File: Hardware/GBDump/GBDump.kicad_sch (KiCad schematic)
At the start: 19 parts, among them J1 Conn_01x06, J2 Micro_SD_Card_Det_Hirose_DM3AT, J3 Conn_01x06, U2 TXB0108PW, U3 TXB0108PW, U4 TXB0108PW, U5 Cartridge_Bus, U6 TXB0108PW

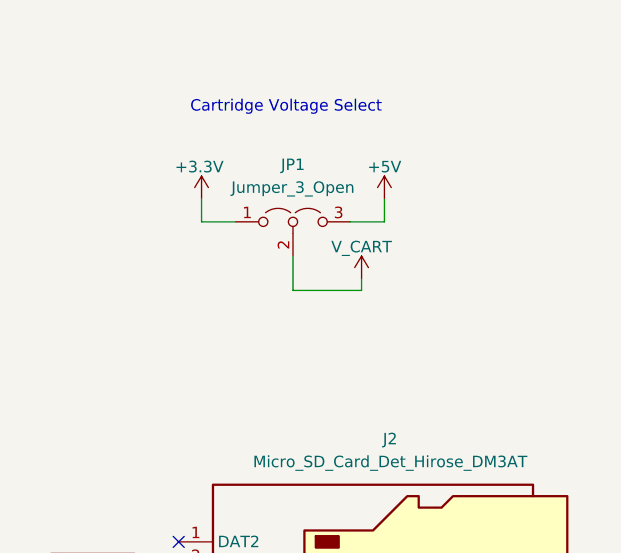
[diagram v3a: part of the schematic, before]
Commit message: Fixed CART_VCC label
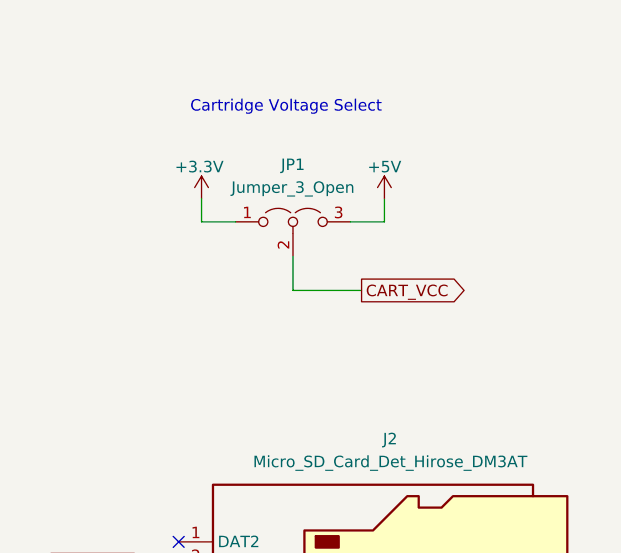
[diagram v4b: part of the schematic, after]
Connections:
- net CART_VCC: now also JP1.2 (C)
- net V_CART: no longer JP1.2 (C)
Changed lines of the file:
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@@
 	(wire
 		(pts
-			(xy 245.11 43.18) (xy 245.11 41.91)
-		)
-		(stroke
-			(width 0)
-			(type default)
-		)
-	)
-	(wire
-		(pts
 			(xy 130.81 78.74) (xy 175.26 78.74)
 		)
@@
 		)
 	)
+	(global_label "CART_VCC"
+		(shape output)
+		(at 245.11 43.18 0)
+		(fields_autoplaced yes)
+		(effects
+			(font
+				(size 1.27 1.27)
+			)
+			(justify left)
+		)
+		(property "Intersheetrefs" "${INTERSHEET_REFS}"
+			(at 257.2876 43.18 0)
+			(effects
+				(font
+					(size 1.27 1.27)
+				)
+				(justify left)
+				(hide yes)
+			)
+		)
+	)
 	(global_label "CART_WR"
 		(shape output)
@@
 					(unit 1)
 				)
-			)
-		)
-	)
-	(symbol
-		(lib_id "power:+3.3V")
-		(at 245.11 41.91 0)
-		(unit 1)
-		(exclude_from_sim no)
-		(in_bom yes)
-		(on_board yes)
-		(dnp no)
-		(property "Reference" "#PWR026"
-			(at 245.11 45.72 0)
-			(effects
-				(font
-					(size 1.27 1.27)
-				)
-				(hide yes)
-			)
-		)
-		(property "Value" "V_CART"
-			(at 245.11 38.354 0)
-			(effects
-				(font
-					(size 1.27 1.27)
-				)
-			)
-		)
-		(property "Footprint" ""
-			(at 245.11 41.91 0)
-			(effects
-				(font
-					(size 1.27 1.27)
-				)
-				(hide yes)
-			)
-		)
-		(property "Datasheet" ""
-			(at 245.11 41.91 0)
-			(effects
-				(font
-					(size 1.27 1.27)
-				)
-				(hide yes)
-			)
-		)
-		(property "Description" "Power symbol creates a global label with name \"+3.3V\""
-			(at 245.11 41.91 0)
-			(effects
-				(font
-					(size 1.27 1.27)
-				)
-				(hide yes)
-			)
-		)
-		(pin "1"
-		)
-		(instances
-			(project "GBDump"
-				(path "/97c582ec-aebc-49f1-a03f-b2d95e3214dc"
-					(reference "#PWR026")
-					(unit 1)
-				)

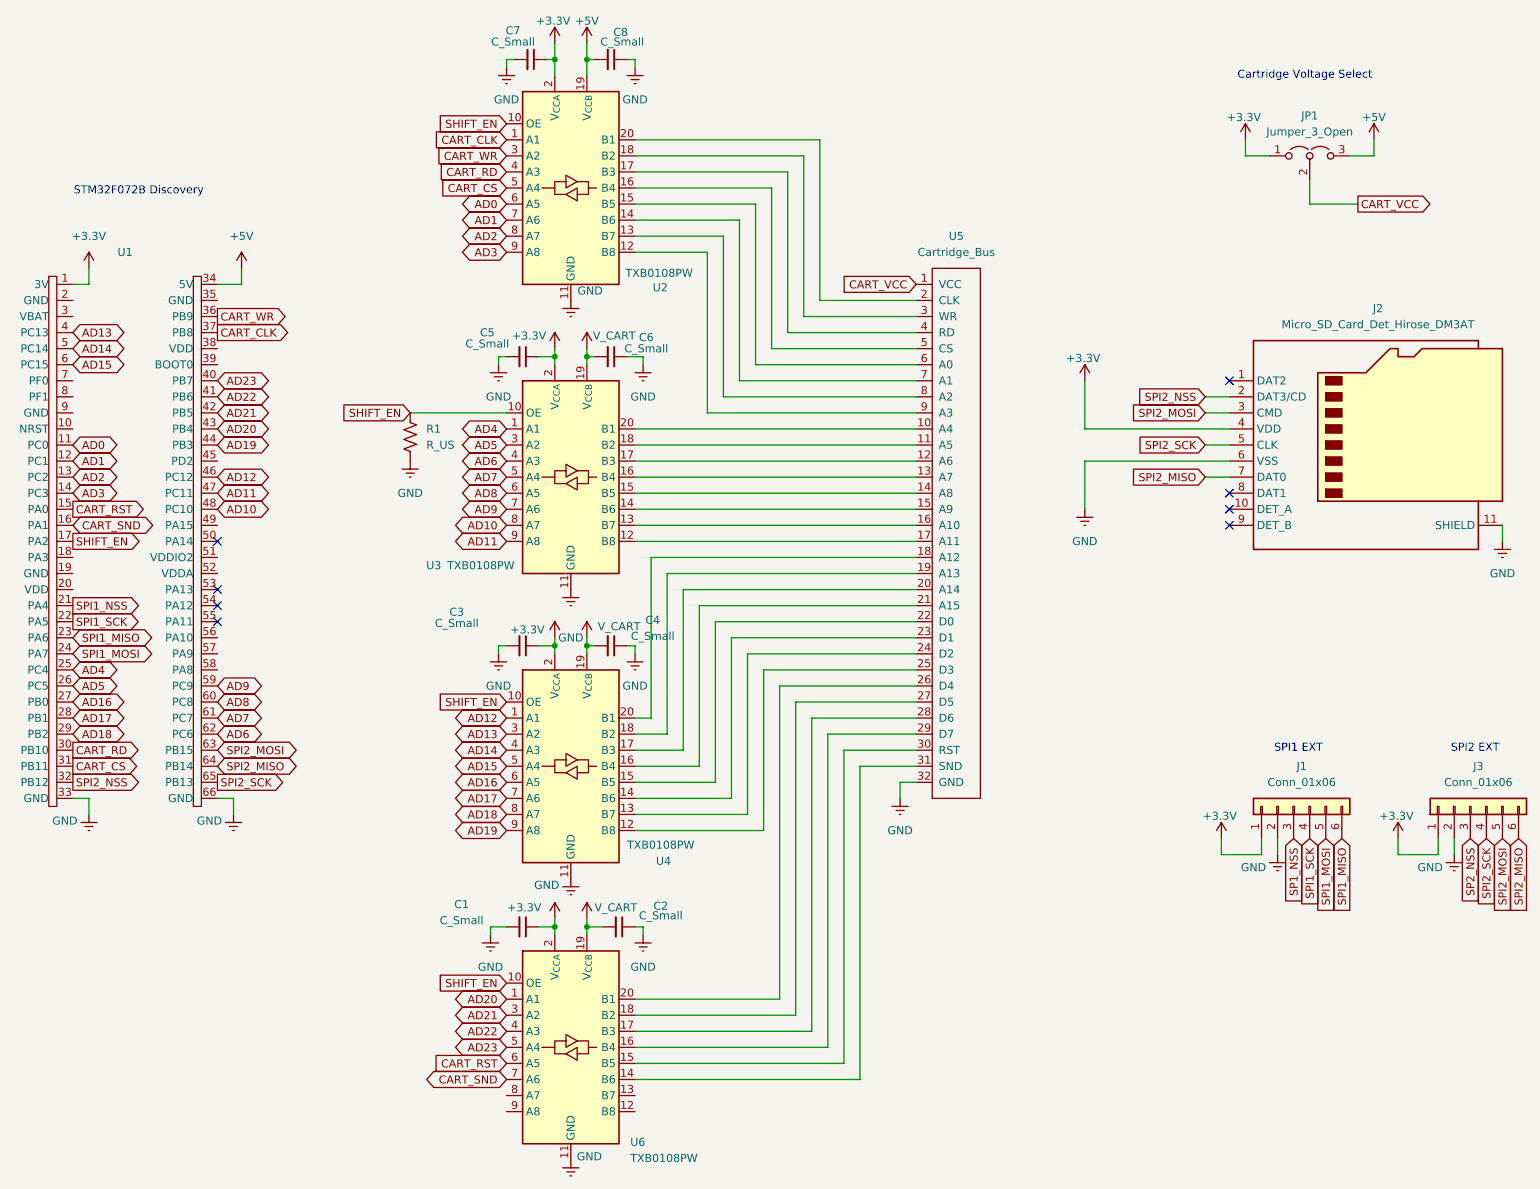
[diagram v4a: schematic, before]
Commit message: Finished board layout and routing, will add silkscreen.
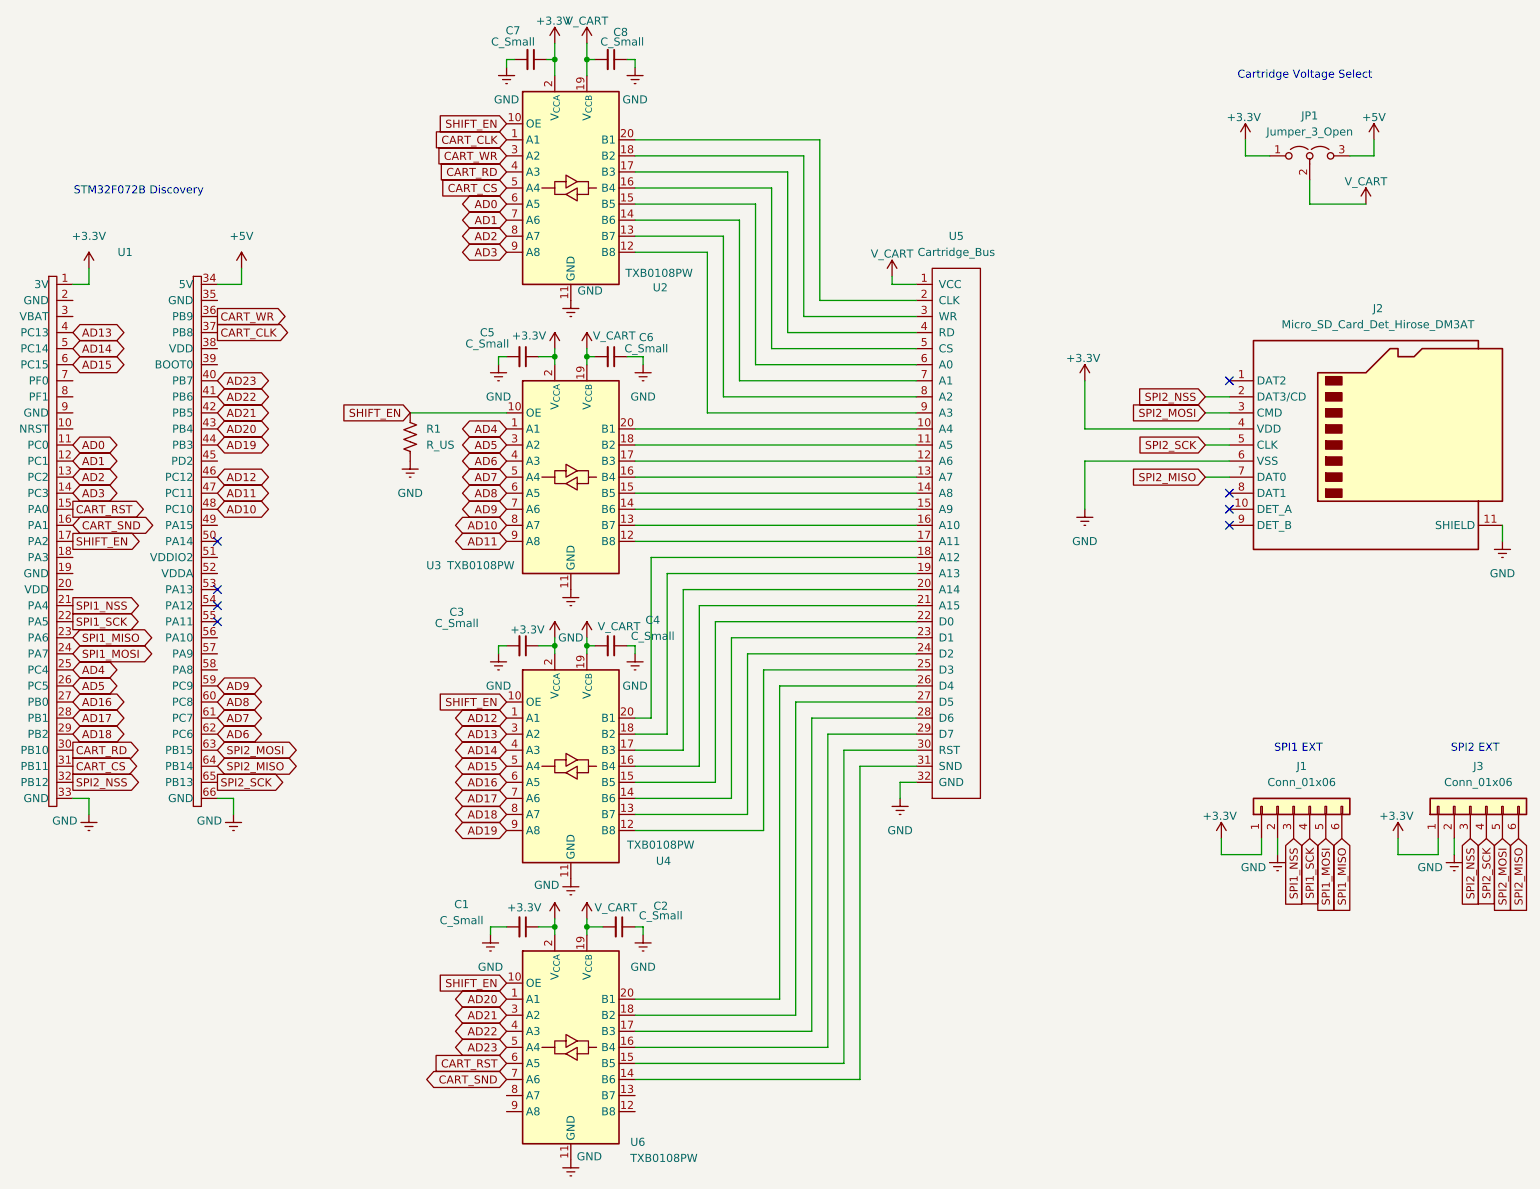
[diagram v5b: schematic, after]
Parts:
- C1, C2, C3, C4, C5, C6, C7, C8: footprint (none) -> Capacitor_SMD:C_1206_3216Metric
- J1, J3: footprint (none) -> Connector_PinHeader_2.54mm:PinHeader_1x06_P2.54mm_Vertical
- J2: footprint (none) -> Connector_Card:microSD_HC_Hirose_DM3AT-SF-PEJM5
- JP1: footprint (none) -> Connector_PinHeader_2.54mm:PinHeader_1x03_P2.54mm_Vertical
- R1: footprint (none) -> Resistor_SMD:R_1206_3216Metric
- U1: footprint (none) -> Connector_PinHeader_2.54mm:STM32F072B-DISCO
- U5: footprint Connector_GameBoy:GameBoy_GamePak_CGB-002_P1.50mm_Edge -> Gameboy:Game_Boy_Advance_Edge_Connector
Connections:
- net CART_VCC is gone; now on net V_CART: JP1.2 (C), U5.1 (VCC)
- net SP1_NSS is gone; now on net SPI1_NSS: J1.3 (Pin_3)
- net SP2_NSS is gone; now on net SPI2_NSS: J3.3 (Pin_3)
- net +5V: no longer C8.2, U2.19 (V_{CCB})
- net V_CART: now also C8.2, U2.19 (V_{CCB})
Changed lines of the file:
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@@
 	(wire
 		(pts
+			(xy 171.45 54.61) (xy 171.45 55.88)
+		)
+		(stroke
+			(width 0)
+			(type default)
+		)
+	)
+	(wire
+		(pts
 			(xy 130.81 78.74) (xy 175.26 78.74)
 		)
@@
 	(wire
 		(pts
-			(xy 237.49 43.18) (xy 245.11 43.18)
+			(xy 237.49 43.18) (xy 246.38 43.18)
 		)
 		(stroke
@@
 	(wire
 		(pts
+			(xy 171.45 55.88) (xy 175.26 55.88)
+		)
+		(stroke
+			(width 0)
+			(type default)
+		)
+	)
+	(wire
+		(pts
 			(xy 154.94 38.1) (xy 154.94 63.5)
 		)
@@
 		)
 	)
-	(global_label "CART_VCC"
-		(shape input)
-		(at 175.26 55.88 180)
-		(fields_autoplaced yes)
-		(effects
-			(font
-				(size 1.27 1.27)
-			)
-			(justify right)
-		)
-		(property "Intersheetrefs" "${INTERSHEET_REFS}"
-			(at 163.0824 55.88 0)
-			(effects
-				(font
-					(size 1.27 1.27)
-				)
-				(justify right)
-				(hide yes)
-			)
-		)
-	)
 	(global_label "SPI2_SCK"
 		(shape input)
@@
 		)
 	)
-	(global_label "CART_VCC"
-		(shape output)
-		(at 245.11 43.18 0)
-		(fields_autoplaced yes)
-		(effects
-			(font
-				(size 1.27 1.27)
-			)
-			(justify left)
-		)
-		(property "Intersheetrefs" "${INTERSHEET_REFS}"
-			(at 257.2876 43.18 0)
-			(effects
-				(font
-					(size 1.27 1.27)
-				)
-				(justify left)
-				(hide yes)
-			)
-		)
-	)
 	(global_label "CART_WR"
 		(shape output)
@@
 		)
 	)
-	(global_label "SP1_NSS"
+	(global_label "SPI1_NSS"
 		(shape input)
 		(at 234.95 143.51 270)
@@
 		)
 		(property "Intersheetrefs" "${INTERSHEET_REFS}"
-			(at 234.95 154.9013 90)
+			(at 234.95 155.5061 90)
 			(effects
 				(font
@@
 		)
 	)
-	(global_label "SP2_NSS"
+	(global_label "SPI2_NSS"
 		(shape input)
 		(at 262.89 143.51 270)
@@
 		)
 		(property "Intersheetrefs" "${INTERSHEET_REFS}"
-			(at 262.89 154.9013 90)
+			(at 262.89 155.5061 90)
 			(effects
 				(font
@@
 			)
 		)
-		(property "Footprint" ""
+		(property "Footprint" "Capacitor_SMD:C_1206_3216Metric"
 			(at 114.3 20.32 0)
 			(effects
@@
 			)
 		)
-		(property "Footprint" ""
+		(property "Footprint" "Capacitor_SMD:C_1206_3216Metric"
 			(at 128.27 157.48 0)
 			(effects
@@
 			)
 		)
-		(property "Footprint" ""
+		(property "Footprint" "Connector_PinHeader_2.54mm:PinHeader_1x06_P2.54mm_Vertical"
 			(at 234.95 138.43 0)
 			(effects
@@
 			)
 		)
-		(property "Footprint" ""
+		(property "Footprint" "Capacitor_SMD:C_1206_3216Metric"
 			(at 127 113.03 0)
 			(effects
@@
 			)
 		)
-		(property "Footprint" ""
+		(property "Footprint" "Capacitor_SMD:C_1206_3216Metric"
 			(at 113.03 113.03 0)
 			(effects
@@
 			)
 		)
-		(property "Value" "+5V"
+		(property "Value" "V_CART"
 			(at 123.19 14.224 0)
 			(effects
@@
 			)
 		)
-		(property "Footprint" ""
+		(property "Footprint" "Connector_PinHeader_2.54mm:PinHeader_1x06_P2.54mm_Vertical"
 			(at 262.89 138.43 0)
 			(effects
@@
 			)
 		)
-		(property "Footprint" "Connector_GameBoy:GameBoy_GamePak_CGB-002_P1.50mm_Edge"
+		(property "Footprint" "Gameboy:Game_Boy_Advance_Edge_Connector"
 			(at 177.8 71.12 0)
 			(effects
@@
 	(symbol
 		(lib_id "power:+3.3V")
+		(at 246.38 43.18 0)
+		(unit 1)
+		(exclude_from_sim no)
+		(in_bom yes)
+		(on_board yes)
+		(dnp no)
+		(property "Reference" "#PWR037"
+			(at 246.38 46.99 0)
+			(effects
+				(font
+					(size 1.27 1.27)
+				)
+				(hide yes)
+			)
+		)
+		(property "Value" "V_CART"
+			(at 246.38 39.624 0)
+			(effects
+				(font
+					(size 1.27 1.27)
+				)
+			)
+		)
+		(property "Footprint" ""
+			(at 246.38 43.18 0)
+			(effects
+				(font
+					(size 1.27 1.27)
+				)
+				(hide yes)
+			)
+		)
+		(property "Datasheet" ""
+			(at 246.38 43.18 0)
+			(effects
+				(font
+					(size 1.27 1.27)
+				)
+				(hide yes)
+			)
+		)
+		(property "Description" "Power symbol creates a global label with name \"+3.3V\""
+			(at 246.38 43.18 0)
+			(effects
+				(font
+					(size 1.27 1.27)
+				)
+				(hide yes)
+			)
+		)
+		(pin "1"
+		)
+		(instances
+			(project "GBDump"
+				(path "/97c582ec-aebc-49f1-a03f-b2d95e3214dc"
+					(reference "#PWR037")
+					(unit 1)
+				)
+			)
+		)
+	)
+	(symbol
+		(lib_id "power:+3.3V")
 		(at 227.33 33.02 0)
 		(unit 1)
@@
 			)
 		)
-		(property "Footprint" ""
+		(property "Footprint" "Connector_PinHeader_2.54mm:STM32F072B-DISCO"
 			(at 41.91 55.88 0)
 			(effects
@@
 			)
 		)
-		(property "Footprint" ""
+		(property "Footprint" "Capacitor_SMD:C_1206_3216Metric"
 			(at 113.03 67.31 0)
 			(effects
@@
 			)
 		)
-		(property "Footprint" ""
+		(property "Footprint" "Capacitor_SMD:C_1206_3216Metric"
 			(at 113.03 157.48 0)
 			(effects
@@
 			)
 		)
-		(property "Footprint" ""
+		(property "Footprint" "Capacitor_SMD:C_1206_3216Metric"
 			(at 127 20.32 0)
 			(effects
@@
 	)
 	(symbol
+		(lib_id "power:+3.3V")
+		(at 171.45 54.61 0)
+		(unit 1)
+		(exclude_from_sim no)
+		(in_bom yes)
+		(on_board yes)
+		(dnp no)
+		(property "Reference" "#PWR026"
+			(at 171.45 58.42 0)
+			(effects
+				(font
+					(size 1.27 1.27)
+				)
+				(hide yes)
+			)
+		)
+		(property "Value" "V_CART"
+			(at 171.45 51.054 0)
+			(effects
+				(font
+					(size 1.27 1.27)
+				)
+			)
+		)
+		(property "Footprint" ""
+			(at 171.45 54.61 0)
+			(effects
+				(font
+					(size 1.27 1.27)
+				)
+				(hide yes)
+			)
+		)
+		(property "Datasheet" ""
+			(at 171.45 54.61 0)
+			(effects
+				(font
+					(size 1.27 1.27)
+				)
+				(hide yes)
+			)
+		)
+		(property "Description" "Power symbol creates a global label with name \"+3.3V\""
+			(at 171.45 54.61 0)
+			(effects
+				(font
+					(size 1.27 1.27)
+				)
+				(hide yes)
+			)
+		)
+		(pin "1"
+		)
+		(instances
+			(project "GBDump"
+				(path "/97c582ec-aebc-49f1-a03f-b2d95e3214dc"
+					(reference "#PWR026")
+					(unit 1)
+				)
+			)
+		)
+	)
+	(symbol
 		(lib_id "power:Earth")
 		(at 67.31 139.7 0)
@@
 			)
 		)
-		(property "Footprint" ""
+		(property "Footprint" "Connector_PinHeader_2.54mm:PinHeader_1x03_P2.54mm_Vertical"
 			(at 237.49 35.56 0)
 			(effects
@@
 			)
 		)
-		(property "Footprint" ""
+		(property "Footprint" "Resistor_SMD:R_1206_3216Metric"
 			(at 96.266 80.264 90)
 			(effects
@@
 			)
 		)
-		(property "Footprint" ""
+		(property "Footprint" "Connector_Card:microSD_HC_Hirose_DM3AT-SF-PEJM5"
 			(at 299.72 63.5 0)
 			(effects
@@
 			)
 		)
-		(property "Footprint" ""
+		(property "Footprint" "Capacitor_SMD:C_1206_3216Metric"
 			(at 127 67.31 0)
 			(effects
